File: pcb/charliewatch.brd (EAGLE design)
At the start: 33 x 33 mm, 85 parts, among them U2 CC430F5137IRGZR, X1 CRYSTALS-NOGND-IQXC-25, X2 FA-128

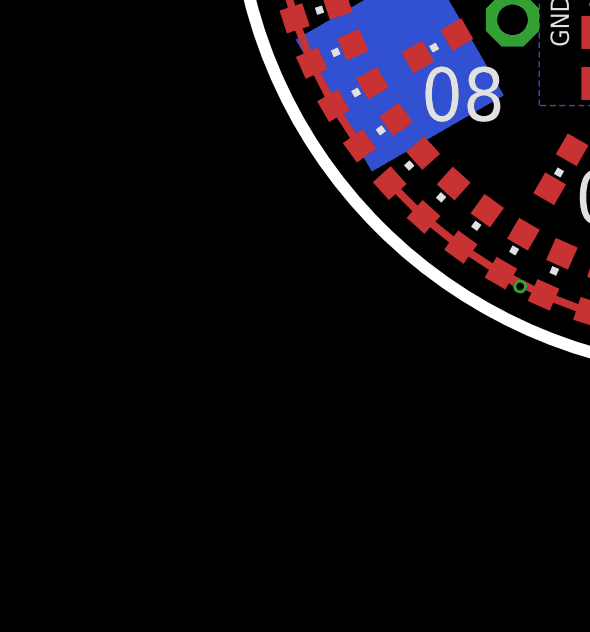
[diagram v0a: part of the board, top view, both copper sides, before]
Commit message: Add LIS3DH Accelerometer
LIS3DH is an i2c accelerometer. Hope to use this to control the watch
with tap based gestures
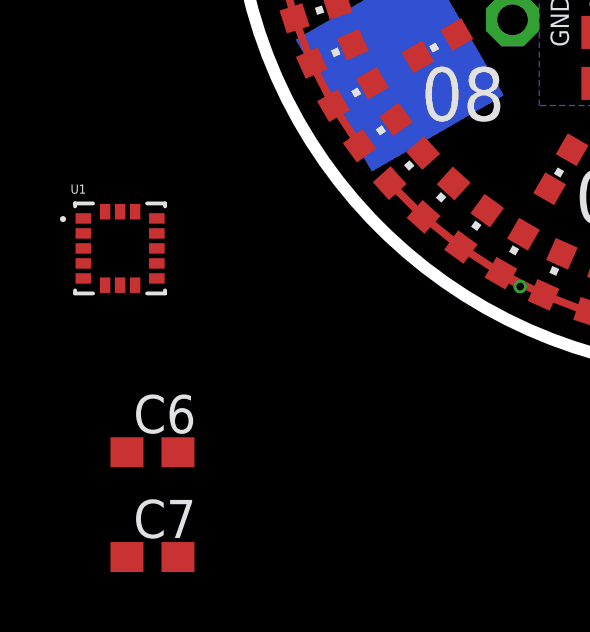
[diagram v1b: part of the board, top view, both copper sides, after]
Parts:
- added C6: 10uF, resistor:C0603
- added C7: 0.1uF, resistor:C0603
- added U1: LIS3DH, LIS3DH:PQFN50P300X300X100-16N
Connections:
- new net IMU_INT: U1.11, U2.13
- new net IMU_SCL: U1.4, U2.11
- new net IMU_SDA: U1.6, U2.10
- net GND: now also C6.2, C7.2, U1.10, U1.12, U1.5, U1.7
- net VCC: now also C6.1, C7.1, U1.1, U1.14, U1.8
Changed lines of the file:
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@@
 <?xml version="1.0" encoding="utf-8"?>
 <!DOCTYPE eagle SYSTEM "eagle.dtd">
-<eagle version="7.7.0">
+<eagle version="9.4.0">
 <drawing>
 <settings>
 <setting alwaysvectorfont="no"/>
+<setting keepoldvectorfont="yes"/>
 <setting verticaltext="up"/>
 </settings>
@@
 <param name="dpMaxLengthDifference" value="10mm"/>
 <param name="dpGapFactor" value="2.5"/>
-<param name="checkGrid" value="0"/>
 <param name="checkAngle" value="0"/>
 <param name="checkFont" value="1"/>
 <param name="checkRestrict" value="1"/>
+<param name="checkStop" value="0"/>
+<param name="checkValues" value="0"/>
+<param name="checkNames" value="1"/>
+<param name="checkWireStubs" value="1"/>
+<param name="checkPolygonWidth" value="0"/>
 <param name="useDiameter" value="13"/>
 <param name="maxErrors" value="50"/>
@@
 <element name="X1" library="IQD-Frequency-Products" package="2.0X1.2-2PAD" value="CRYSTALS-NOGND-IQXC-25" x="24.4475" y="31.115" smashed="yes" rot="R180"/>
 <element name="U2" library="Texas Instruments_By_element14_Batch_1" package="QFN50P700X700X100-49N" value="CC430F5137IRGZR" x="25.4" y="25.4" smashed="yes">
+<attribute name="MPN" value="CC430F5137IRGZR" x="25.4" y="25.4" size="1.778" layer="27" display="off"/>
+<attribute name="OC_FARNELL" value="-" x="25.4" y="25.4" size="1.778" layer="27" display="off"/>
+<attribute name="OC_NEWARK" value="68R5912" x="25.4" y="25.4" size="1.778" layer="27" display="off"/>
 <attribute name="PACKAGE" value="QFN-48" x="25.4" y="25.4" size="1.778" layer="27" display="off"/>
 <attribute name="SUPPLIER" value="TEXAS INSTRUMENTS" x="25.4" y="25.4" size="1.778" layer="27" display="off"/>
-<attribute name="OC_FARNELL" value="-" x="25.4" y="25.4" size="1.778" layer="27" display="off"/>
-<attribute name="MPN" value="CC430F5137IRGZR" x="25.4" y="25.4" size="1.778" layer="27" display="off"/>
-<attribute name="OC_NEWARK" value="68R5912" x="25.4" y="25.4" size="1.778" layer="27" display="off"/>
 </element>
 <element name="R1" library="rcl" package="R0603" value="75k" x="27.94" y="31.115" smashed="yes" rot="R180">
@@
 <element name="JP1" library="adafruit" package="1X06-BIGLOCK" value="" x="18.034" y="26.9875" smashed="yes" rot="MR90">
 <attribute name="VALUE" x="14.859" y="19.3675" size="1.27" layer="28" rot="MR90"/>
+</element>
+<element name="U1" library="LIS3DH" package="PQFN50P300X300X100-16N" value="LIS3DH" x="5.08" y="13.0175" smashed="yes">
+<attribute name="AVAILABILITY" value="Unavailable" x="5.08" y="13.0175" size="1.778" layer="27" display="off"/>
+<attribute name="DESCRIPTION" value=" MEMS digital output motion sensor ultra low-power high performance 3-axes nano accelerometer " x="5.08" y="13.0175" size="1.778" layer="27" display="off"/>
+<attribute name="MF" value="STMicroelectronics" x="5.08" y="13.0175" size="1.778" layer="27" display="off"/>
+<attribute name="MP" value="LIS3DH" x="5.08" y="13.0175" size="1.778" layer="27" display="off"/>
+<attribute name="NAME" x="3.4288" y="14.84171875" size="0.3048375" layer="25"/>
+<attribute name="PACKAGE" value="LGA-16 STMicroelectronics" x="5.08" y="13.0175" size="1.778" layer="27" display="off"/>
+<attribute name="PRICE" value="None" x="5.08" y="13.0175" size="1.778" layer="27" display="off"/>
+<attribute name="VALUE" x="3.3491" y="10.83536875" size="0.304959375" layer="27"/>
+</element>
+<element name="C6" library="resistor" package="C0603" value="10uF" x="6.1595" y="6.223" smashed="yes">
+<attribute name="NAME" x="5.5245" y="6.858" size="1.27" layer="25"/>
+<attribute name="VALUE" x="5.5245" y="4.318" size="1.27" layer="27"/>
+</element>
+<element name="C7" library="resistor" package="C0603" value="0.1uF" x="6.1595" y="2.7305" smashed="yes">
+<attribute name="NAME" x="5.5245" y="3.3655" size="1.27" layer="25"/>
+<attribute name="VALUE" x="5.5245" y="0.8255" size="1.27" layer="27"/>
 </element>
 </elements>
@@
 <wire x1="33.9725" y1="24.13" x2="32.9175" y2="22.86" width="0.254" layer="1"/>
 <contactref element="JP1" pad="1"/>
+<contactref element="U1" pad="5"/>
+<contactref element="U1" pad="10"/>
+<contactref element="U1" pad="12"/>
+<contactref element="C7" pad="2"/>
+<contactref element="C6" pad="2"/>
+<contactref element="U1" pad="7"/>
+<wire x1="32.6" y1="27.725" x2="32.6" y2="26.25" width="0" layer="19" extent="1-1"/>
+<wire x1="28.8925" y1="21.2725" x2="32.7025" y2="21.9075" width="0" layer="19" extent="1-1"/>
+<wire x1="26.9875" y1="24.4475" x2="28.8925" y2="21.2725" width="0" layer="19" extent="1-1"/>
+<wire x1="20.955" y1="18.5175" x2="23.495" y2="23.1775" width="0" layer="19" extent="1-1"/>
 <wire x1="18.161" y1="20.6375" x2="20.955" y2="18.5175" width="0" layer="19" extent="1-1"/>
+<wire x1="6.305" y1="13.5175" x2="18.161" y2="20.6375" width="0" layer="19" extent="1-1"/>
+<wire x1="6.305" y1="12.5175" x2="6.305" y2="13.5175" width="0" layer="19" extent="1-1"/>
+<wire x1="5.08" y1="11.7925" x2="6.305" y2="12.5175" width="0" layer="19" extent="1-1"/>
+<wire x1="3.855" y1="12.0175" x2="5.08" y2="11.7925" width="0" layer="19" extent="1-1"/>
+<wire x1="7.0095" y1="6.223" x2="5.08" y2="11.7925" width="0" layer="19" extent="1-1"/>
+<wire x1="7.0095" y1="2.7305" x2="7.0095" y2="6.223" width="0" layer="19" extent="1-1"/>
 </signal>
 <signal name="VCC">
@@
 <via x="33.655" y="32.385" extent="1-16" drill="0.254"/>
 <contactref element="U$1" pad="+$1"/>
+<contactref element="U1" pad="14"/>
+<contactref element="U1" pad="1"/>
+<contactref element="C7" pad="1"/>
+<contactref element="C6" pad="1"/>
+<contactref element="U1" pad="8"/>
 <wire x1="33.655" y1="32.385" x2="36.398525" y2="31.75" width="0" layer="19" extent="16-16"/>
 <wire x1="32.7025" y1="30.48" x2="32.7025" y2="29.9475" width="0" layer="19" extent="1-1"/>
+<wire x1="5.58" y1="14.2425" x2="24.1554" y2="28.8798" width="0" layer="19" extent="1-1"/>
+<wire x1="3.855" y1="14.0175" x2="5.58" y2="14.2425" width="0" layer="19" extent="1-1"/>
+<wire x1="5.58" y1="11.7925" x2="5.58" y2="14.2425" width="0" layer="19" extent="1-1"/>
+<wire x1="5.3095" y1="6.223" x2="5.58" y2="11.7925" width="0" layer="19" extent="1-1"/>
+<wire x1="5.3095" y1="2.7305" x2="5.3095" y2="6.223" width="0" layer="19" extent="1-1"/>
 </signal>
 <signal name="BSL_RST">
@@
 <wire x1="18.161" y1="25.7175" x2="21.9202" y2="24.638" width="0" layer="19" extent="1-1"/>
 </signal>
+<signal name="IMU_INT">
+<contactref element="U1" pad="11"/>
+<contactref element="U2" pad="13"/>
+<wire x1="6.305" y1="13.0175" x2="22.6568" y2="21.9202" width="0" layer="19" extent="1-1"/>
+</signal>
+<signal name="IMU_SCL">
+<contactref element="U1" pad="4"/>
+<contactref element="U2" pad="11"/>
+<wire x1="3.855" y1="12.5175" x2="21.9202" y2="23.1394" width="0" layer="19" extent="1-1"/>
+</signal>
+<signal name="IMU_SDA">
+<contactref element="U1" pad="6"/>
+<contactref element="U2" pad="10"/>
+<wire x1="4.58" y1="11.7925" x2="21.9202" y2="23.6474" width="0" layer="19" extent="1-1"/>
+</signal>
 </signals>
+<mfgpreviewcolors>
+<mfgpreviewcolor name="soldermaskcolor" color="0xC8008000"/>
+<mfgpreviewcolor name="silkscreencolor" color="0xFFFEFEFE"/>
+<mfgpreviewcolor name="backgroundcolor" color="0xFF282828"/>
+<mfgpreviewcolor name="coppercolor" color="0xFFFFBF00"/>
+<mfgpreviewcolor name="substratecolor" color="0xFF786E46"/>
+</mfgpreviewcolors>
 <errors>
 </errors>
